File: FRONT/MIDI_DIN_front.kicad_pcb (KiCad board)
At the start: 2 copper layers, 30 x 128.5 mm, 6 parts, among them J1 Screw_Terminal_01x01, J2 Screw_Terminal_01x01, J3 Screw_Terminal_01x01, J4 Screw_Terminal_01x01

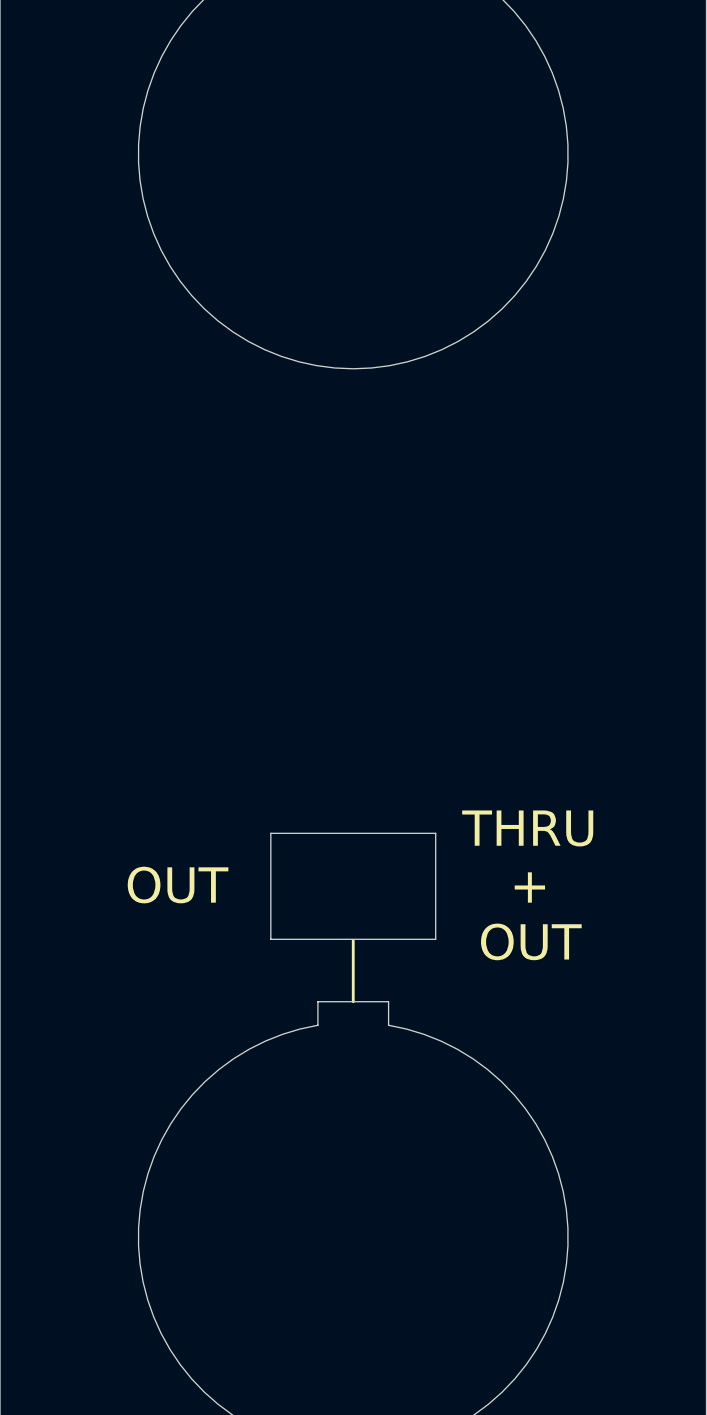
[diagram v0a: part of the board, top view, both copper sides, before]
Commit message: Add custom symbols and footprints
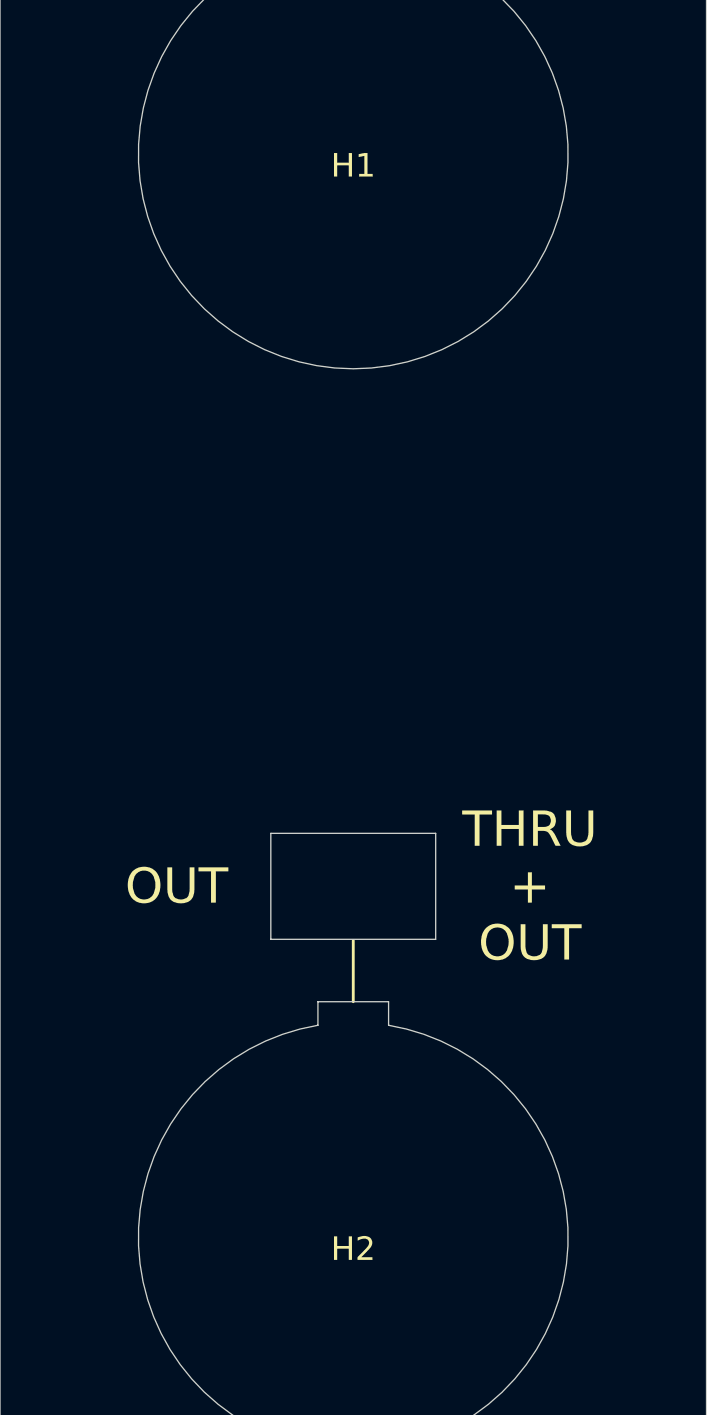
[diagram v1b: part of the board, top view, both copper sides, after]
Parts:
- H1, H2: footprint CustomLib:DIN_Hole_Hirschmann -> Custom_FP:DIN_Hole_Hirschmann
- J1, J2, J3, J4: footprint CustomLib:Wide_M3 -> Custom_FP:Wide_M3
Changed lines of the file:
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@@
-(kicad_pcb (version 20171130) (host pcbnew "(5.1.6)-1")
+(kicad_pcb (version 20171130) (host pcbnew "(5.1.10)-1")
   (general
     (thickness 1.6)
@@
     (add_net GND)
   )
-  (module CustomLib:DIN_Hole_Hirschmann (layer F.Cu)
+  (module Custom_FP:Wide_M3 (layer F.Cu)
+    (at 82.5 43)
+    (fp_text reference J4 (at 0 -3.81) (layer F.SilkS) hide
+      (effects (font (size 1 1) (thickness 0.15)))
+    )
+    (fp_text value Screw_Terminal_01x01 (at 0 3.81) (layer F.Fab)
+      (effects (font (size 1 1) (thickness 0.15)))
+    )
+    (pad 1 thru_hole oval (at 0 0) (size 9.2 4.2) (drill oval 8.2 3.2) (layers *.Cu *.Mask)
+      (net 1 GND))
+  )
+  (module Custom_FP:Wide_M3 (layer F.Cu)
+    (at 82.5 165.5)
+    (fp_text reference J3 (at 0 -3.81) (layer F.SilkS) hide
+      (effects (font (size 1 1) (thickness 0.15)))
+    )
+    (fp_text value Screw_Terminal_01x01 (at 0 3.81) (layer F.Fab)
+      (effects (font (size 1 1) (thickness 0.15)))
+    )
+    (pad 1 thru_hole oval (at 0 0) (size 9.2 4.2) (drill oval 8.2 3.2) (layers *.Cu *.Mask)
+      (net 1 GND))
+  )
+  (module Custom_FP:Wide_M3 (layer F.Cu)
+    (at 97.5 43)
+    (fp_text reference J2 (at 0 -3.81) (layer F.SilkS) hide
+      (effects (font (size 1 1) (thickness 0.15)))
+    )
+    (fp_text value Screw_Terminal_01x01 (at 0 3.81) (layer F.Fab)
+      (effects (font (size 1 1) (thickness 0.15)))
+    )
+    (pad 1 thru_hole oval (at 0 0) (size 9.2 4.2) (drill oval 8.2 3.2) (layers *.Cu *.Mask)
+      (net 1 GND))
+  )
+  (module Custom_FP:Wide_M3 (layer F.Cu)
+    (at 97.5 165.5)
+    (fp_text reference J1 (at 0 -3.81) (layer F.SilkS) hide
+      (effects (font (size 1 1) (thickness 0.15)))
+    )
+    (fp_text value Screw_Terminal_01x01 (at 0 3.81) (layer F.Fab)
+      (effects (font (size 1 1) (thickness 0.15)))
+    )
+    (pad 1 thru_hole oval (at 0 0) (size 9.2 4.2) (drill oval 8.2 3.2) (layers *.Cu *.Mask)
+      (net 1 GND))
+  )
+  (module Custom_FP:DIN_Hole_Hirschmann (layer F.Cu)
     (at 90 135.5)
-    (fp_text reference H2 (at 0 0.5) (layer F.SilkS) hide
+    (fp_text reference H2 (at 0 0.5) (layer F.SilkS)
       (effects (font (size 1 1) (thickness 0.15)))
     )
@@
       (effects (font (size 1 1) (thickness 0.15)))
     )
+    (fp_arc (start 0 0) (end -1.499999 -8.95) (angle -341.1) (layer Dwgs.User) (width 0.12))
     (fp_circle (center 0 0) (end 10 0) (layer F.Fab) (width 0.12))
     (fp_line (start -1.5 -10) (end -1.499999 -8.95) (layer Dwgs.User) (width 0.12))
@@
     (fp_line (start 0 10.25) (end 0 14.25) (layer Dwgs.User) (width 0.12))
     (fp_line (start -0.25 14.25) (end 0.25 14.25) (layer Dwgs.User) (width 0.12))
-    (fp_arc (start 0 0) (end -1.499999 -8.95) (angle -341.1) (layer Dwgs.User) (width 0.12))
   )
-  (module CustomLib:DIN_Hole_Hirschmann (layer F.Cu)
+  (module Custom_FP:DIN_Hole_Hirschmann (layer F.Cu)
     (at 90 89.5)
-    (fp_text reference H1 (at 0 0.5) (layer F.SilkS) hide
+    (fp_text reference H1 (at 0 0.5) (layer F.SilkS)
       (effects (font (size 1 1) (thickness 0.15)))
     )
@@
       (effects (font (size 1 1) (thickness 0.15)))
     )
+    (fp_arc (start 0 0) (end -1.499999 -8.95) (angle -341.1) (layer Dwgs.User) (width 0.12))
     (fp_circle (center 0 0) (end 10 0) (layer F.Fab) (width 0.12))
     (fp_line (start -1.5 -10) (end -1.499999 -8.95) (layer Dwgs.User) (width 0.12))
@@
     (fp_line (start 0 10.25) (end 0 14.25) (layer Dwgs.User) (width 0.12))
     (fp_line (start -0.25 14.25) (end 0.25 14.25) (layer Dwgs.User) (width 0.12))
-    (fp_arc (start 0 0) (end -1.499999 -8.95) (angle -341.1) (layer Dwgs.User) (width 0.12))
-  )
-  (module CustomLib:Wide_M3 (layer F.Cu)
-    (at 97.5 165.5)
-    (fp_text reference J1 (at 0 -3.81) (layer F.SilkS) hide
-      (effects (font (size 1 1) (thickness 0.15)))
-    )
-    (fp_text value Screw_Terminal_01x01 (at 0 3.81) (layer F.Fab)
-      (effects (font (size 1 1) (thickness 0.15)))
-    )
-    (pad 1 thru_hole oval (at 0 0) (size 9.2 4.2) (drill oval 8.2 3.2) (layers *.Cu *.Mask)
-      (net 1 GND))
-  )
-  (module CustomLib:Wide_M3 (layer F.Cu)
-    (at 97.5 43)
-    (fp_text reference J2 (at 0 -3.81) (layer F.SilkS) hide
-      (effects (font (size 1 1) (thickness 0.15)))
-    )
-    (fp_text value Screw_Terminal_01x01 (at 0 3.81) (layer F.Fab)
-      (effects (font (size 1 1) (thickness 0.15)))
-    )
-    (pad 1 thru_hole oval (at 0 0) (size 9.2 4.2) (drill oval 8.2 3.2) (layers *.Cu *.Mask)
-      (net 1 GND))
-  )
-  (module CustomLib:Wide_M3 (layer F.Cu)
-    (at 82.5 165.5)
-    (fp_text reference J3 (at 0 -3.81) (layer F.SilkS) hide
-      (effects (font (size 1 1) (thickness 0.15)))
-    )
-    (fp_text value Screw_Terminal_01x01 (at 0 3.81) (layer F.Fab)
-      (effects (font (size 1 1) (thickness 0.15)))
-    )
-    (pad 1 thru_hole oval (at 0 0) (size 9.2 4.2) (drill oval 8.2 3.2) (layers *.Cu *.Mask)
-      (net 1 GND))
-  )
-  (module CustomLib:Wide_M3 (layer F.Cu)
-    (at 82.5 43)
-    (fp_text reference J4 (at 0 -3.81) (layer F.SilkS) hide
-      (effects (font (size 1 1) (thickness 0.15)))
-    )
-    (fp_text value Screw_Terminal_01x01 (at 0 3.81) (layer F.Fab)
-      (effects (font (size 1 1) (thickness 0.15)))
-    )
-    (pad 1 thru_hole oval (at 0 0) (size 9.2 4.2) (drill oval 8.2 3.2) (layers *.Cu *.Mask)
-      (net 1 GND))
   )
   (gr_circle (center 93.5 147.75) (end 95.024 147.75) (layer Dwgs.User) (width 0.15))
